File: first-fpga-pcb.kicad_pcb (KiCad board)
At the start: 4 copper layers, 34 parts, among them U1 iCE40-HX1K-VQ100, U2 W25Q128JVS, U3 TLV73312PDBV, U4 TLV73333PDBV, X1 SiT2001B

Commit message: neaten schematic
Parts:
- added C16: 100n, Capacitor_SMD:C_0805_2012Metric, F.Cu at (219.5, 87.8)
- added C17: 100n, Capacitor_SMD:C_0805_2012Metric, F.Cu at (215.1, 90.8)
- added C18: 100n, Capacitor_SMD:C_0805_2012Metric, F.Cu at (230.3, 75.1)
- added C19: 100n, Capacitor_SMD:C_0805_2012Metric, F.Cu at (225.9, 78.1)
- added D3: LED, LED_SMD:LED_0805_2012Metric, F.Cu at (189.4, 92.9)
- added D4: LED, LED_SMD:LED_0805_2012Metric, F.Cu at (215.1, 87.8)
- added D5: LED, LED_SMD:LED_0805_2012Metric, F.Cu at (225.9, 75.1)
- added J1: Conn_01x02, Connector_PinHeader_2.54mm:PinHeader_2x01_P2.54mm_Vertical, F.Cu at (226.0, 71.3)
- added J2: Conn_01x08, Connector_PinHeader_2.54mm:PinHeader_1x08_P2.54mm_Vertical, F.Cu at (189.4, 71.3)
- added J3: Conn_02x06_Top_Bottom, Connector_PinHeader_2.54mm:PinHeader_2x06_P2.54mm_Horizontal, F.Cu at (194.1, 71.3)
- added J4: Conn_02x06_Top_Bottom, Connector_PinHeader_2.54mm:PinHeader_2x06_P2.54mm_Horizontal, F.Cu at (210.0, 71.3)
- added R10: 10k, Resistor_SMD:R_0805_2012Metric, F.Cu at (215.1, 93.8)
- added R11: 10k, Resistor_SMD:R_0805_2012Metric, F.Cu at (230.3, 78.1)
- added R12: 200R, Resistor_SMD:R_0805_2012Metric, F.Cu at (219.5, 90.8)
- added R13: 200R, Resistor_SMD:R_0805_2012Metric, F.Cu at (225.9, 84.0)
- added R9: 22R, Resistor_SMD:R_0805_2012Metric, F.Cu at (225.9, 81.1)
- added SW1: SW_Push, Button_Switch_THT:SW_PUSH_6mm, F.Cu at (204.3, 88.3)
- added SW2: SW_Push, Button_Switch_THT:SW_PUSH_6mm, F.Cu at (193.8, 88.3)
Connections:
- net /reset renamed Net-(U1-Pad89)
- net Net-(D1-Pad2) renamed /cdone
- net Net-(R8-Pad1) renamed /creset
- C10 pad 1: +3V3 -> +1V2
- C11 pad 1: +3V3 -> +1V2
- C8 pad 1: +3V3 -> +1V2
- C9 pad 1: +3V3 -> +1V2
- U1 pad 1: Net-(U1-Pad1) -> /p2_1
- U1 pad 10: Net-(U1-Pad10) -> /p2_10
- U1 pad 2: Net-(U1-Pad2) -> /p2_2
- U1 pad 3: Net-(U1-Pad3) -> /p2_3
- U1 pad 4: Net-(U1-Pad4) -> /p2_4
- U1 pad 51: Net-(U1-Pad51) -> /p1_1
- U1 pad 52: Net-(U1-Pad52) -> /p1_2
- U1 pad 53: Net-(U1-Pad53) -> /p1_3
- U1 pad 54: Net-(U1-Pad54) -> /p1_4
- U1 pad 56: Net-(U1-Pad56) -> /p1_7
- U1 pad 57: Net-(U1-Pad57) -> /p1_8
- U1 pad 59: Net-(U1-Pad59) -> /p1_9
- U1 pad 60: Net-(U1-Pad60) -> /p1_10
- U1 pad 7: Net-(U1-Pad7) -> /p2_7
- U1 pad 78: Net-(U1-Pad78) -> /button1
- U1 pad 79: Net-(U1-Pad79) -> /button2
- U1 pad 8: Net-(U1-Pad8) -> /p2_8
- U1 pad 80: Net-(U1-Pad80) -> /led1
- U1 pad 81: Net-(U1-Pad81) -> /led2
- U1 pad 9: Net-(U1-Pad9) -> /p2_9
- U4 pad 2: Net-(U4-Pad2) -> GND

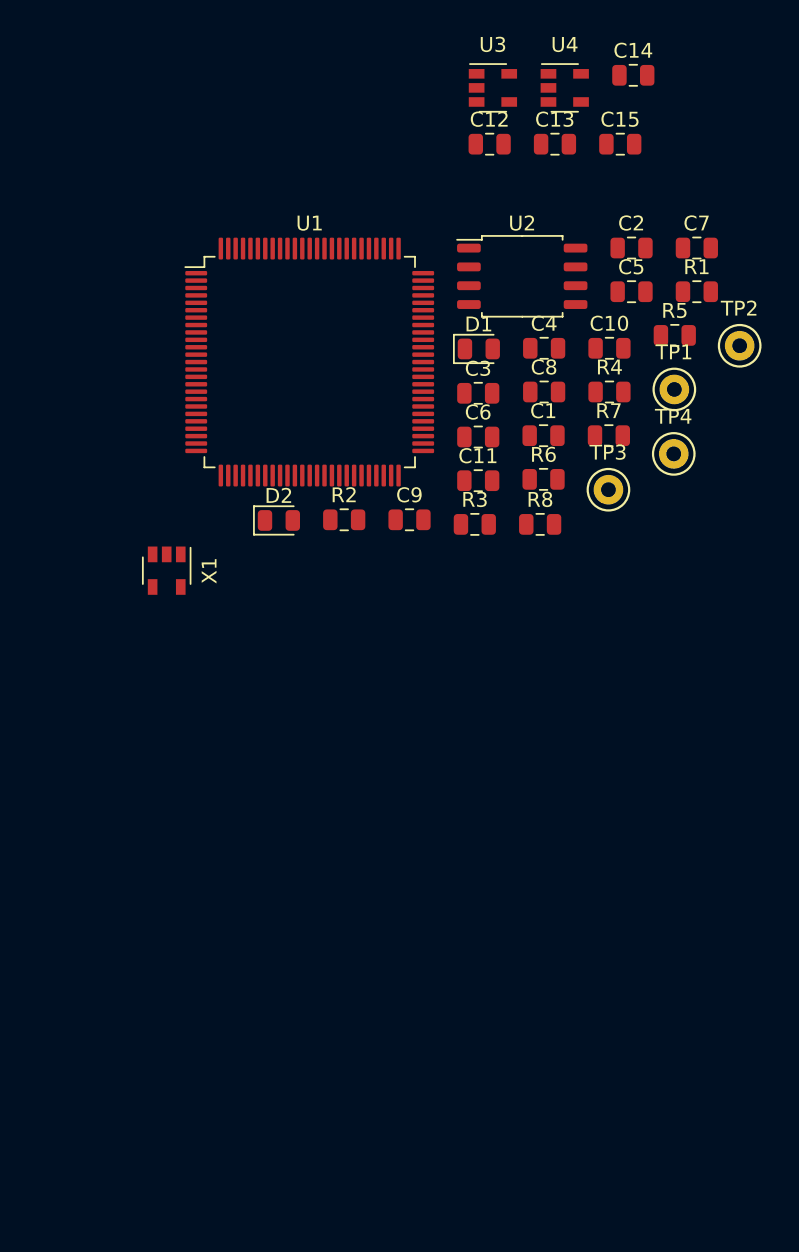
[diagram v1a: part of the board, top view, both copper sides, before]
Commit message: changed to 144 pin package for PLL, added more PMODs, chose FLASH part, updated README
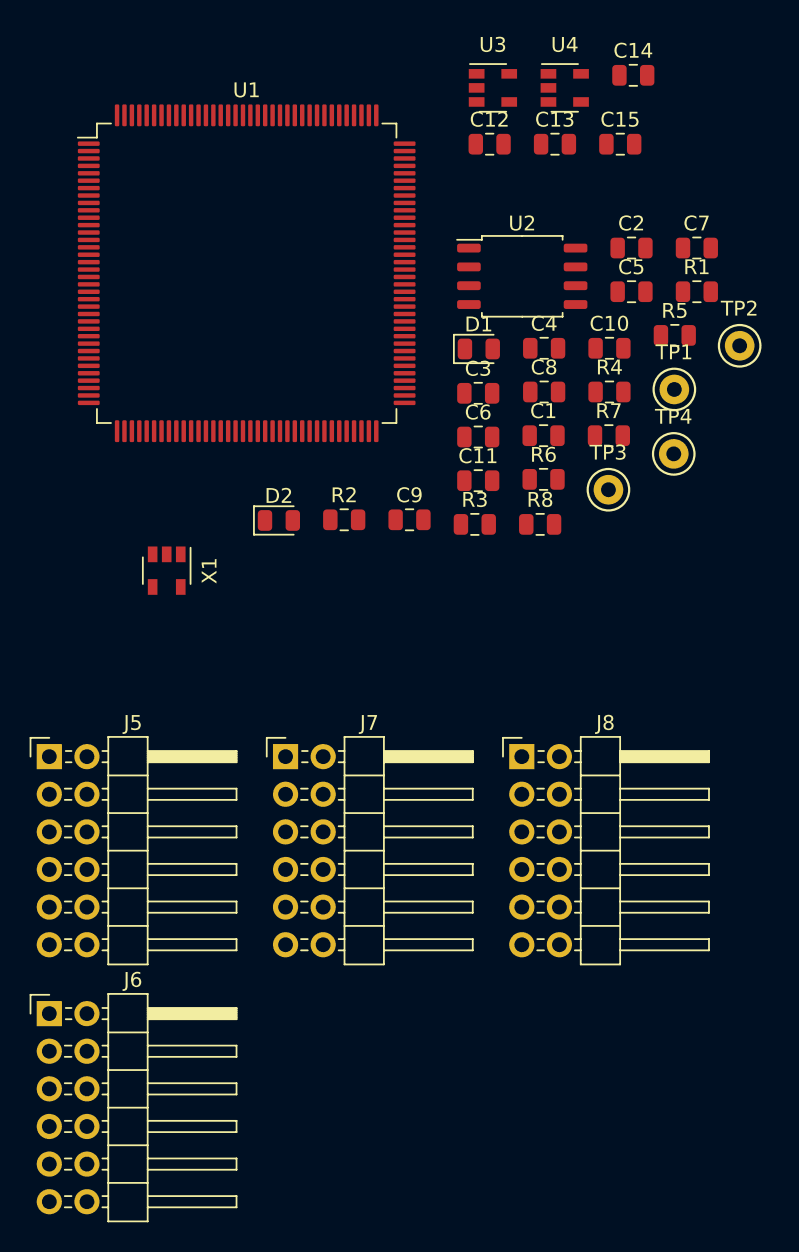
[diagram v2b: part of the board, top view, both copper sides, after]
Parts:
- added J5: Conn_02x06_Top_Bottom, Connector_PinHeader_2.54mm:PinHeader_2x06_P2.54mm_Horizontal, F.Cu at (134.1, 106.4)
- added J6: Conn_02x06_Top_Bottom, Connector_PinHeader_2.54mm:PinHeader_2x06_P2.54mm_Horizontal, F.Cu at (134.1, 123.7)
- added J7: Conn_02x06_Top_Bottom, Connector_PinHeader_2.54mm:PinHeader_2x06_P2.54mm_Horizontal, F.Cu at (150.1, 106.4)
- added J8: Conn_02x06_Top_Bottom, Connector_PinHeader_2.54mm:PinHeader_2x06_P2.54mm_Horizontal, F.Cu at (166.0, 106.4)
- R6: value 22R -> 200R
- U1: value iCE40-HX1K-VQ100 -> iCE40-HX1K-TQ144; footprint Package_QFP:VQFP-100_14x14mm_P0.5mm -> Package_QFP:TQFP-144_20x20mm_P0.5mm
- U2: value W25Q128JVS -> IS25LP016D-JBLE
- moved U1 7.35 mm to (147.5, 73.8)
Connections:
- U1 pad 1: /p2_1 -> /p3_1
- U1 pad 10: /p2_10 -> /p3_10
- U1 pad 100: Net-(U1-Pad100) -> +3V3
- U1 pad 11: +1V2 -> /p4_1
- U1 pad 12: Net-(U1-Pad12) -> /p4_2
- U1 pad 13: Net-(U1-Pad13) -> GND
- U1 pad 14: +3V3 -> GND
- U1 pad 17: GND -> Net-(U1-Pad17)
- U1 pad 19: Net-(U1-Pad19) -> /p4_3
- U1 pad 2: /p2_2 -> /p3_2
- U1 pad 20: Net-(U1-Pad20) -> /p4_4
- U1 pad 21: Net-(U1-Pad21) -> /p4_7
- U1 pad 22: +3V3 -> /p4_8
- U1 pad 23: GND -> /p4_9
- U1 pad 24: Net-(U1-Pad24) -> /p4_10
- U1 pad 27: Net-(U1-Pad27) -> +1V2
- U1 pad 3: /p2_3 -> /p3_3
- U1 pad 30: Net-(U1-Pad30) -> +3V3
- U1 pad 31: +3V3 -> Net-(U1-Pad31)
- U1 pad 32: GND -> Net-(U1-Pad32)
- U1 pad 33: Net-(TP1-Pad1) -> Net-(U1-Pad33)
- U1 pad 34: Net-(TP2-Pad1) -> Net-(U1-Pad34)
- U1 pad 35: +1V2 -> GND
- U1 pad 36: Net-(U1-Pad36) -> +1V2
- U1 pad 38: +3V3 -> Net-(U1-Pad38)
- U1 pad 39: GND -> Net-(U1-Pad39)
- U1 pad 4: /p2_4 -> /p3_4
- U1 pad 41: Net-(TP3-Pad1) -> Net-(U1-Pad41)
- U1 pad 42: Net-(TP4-Pad1) -> Net-(U1-Pad42)
- U1 pad 43: /cdone -> Net-(U1-Pad43)
- U1 pad 44: /creset -> Net-(TP1-Pad1)
- U1 pad 45: /sdo -> Net-(TP2-Pad1)
- U1 pad 46: /sdi -> +3V3
- U1 pad 47: GND -> Net-(U1-Pad47)
- U1 pad 48: /sd_clk -> Net-(U1-Pad48)
- U1 pad 49: /sd_cs -> Net-(U1-Pad49)
- U1 pad 50: +3V3 -> Net-(U1-Pad50)
- U1 pad 51: /p1_1 -> +1V2
- U1 pad 52: /p1_2 -> Net-(U1-Pad52)
- U1 pad 53: /p1_3 -> Net-(U1-Pad53)
- U1 pad 54: /p1_4 -> Net-(U1-Pad54)
- U1 pad 55: GND -> Net-(U1-Pad55)
- U1 pad 56: /p1_7 -> Net-(U1-Pad56)
- U1 pad 57: /p1_8 -> +3V3
- U1 pad 58: +3V3 -> Net-(U1-Pad58)
- U1 pad 59: /p1_9 -> GND
- U1 pad 60: /p1_10 -> Net-(U1-Pad60)
- U1 pad 61: +1V2 -> Net-(U1-Pad61)
- U1 pad 63: Net-(U1-Pad63) -> Net-(TP3-Pad1)
- U1 pad 64: Net-(U1-Pad64) -> Net-(TP4-Pad1)
- U1 pad 65: Net-(U1-Pad65) -> /cdone
- U1 pad 66: Net-(U1-Pad66) -> /creset
- U1 pad 67: +3V3 -> /sdo
- U1 pad 68: Net-(U1-Pad68) -> /sdi
- U1 pad 69: Net-(U1-Pad69) -> GND
- U1 pad 7: /p2_7 -> /p3_7
- U1 pad 70: GND -> /sd_clk
- U1 pad 71: Net-(U1-Pad71) -> /sd_cs
- U1 pad 72: Net-(U1-Pad72) -> +3V3
- U1 pad 73: Net-(U1-Pad73) -> /button1
- U1 pad 74: Net-(U1-Pad74) -> /button2
- U1 pad 75: Net-(D2-Pad1) -> /led1
- U1 pad 76: Net-(U1-Pad76) -> /led2
- U1 pad 77: +1V2 -> Net-(U1-Pad77)
- U1 pad 78: /button1 -> /p5_1
- U1 pad 79: /button2 -> /p5_2
- U1 pad 8: /p2_8 -> /p3_8
- U1 pad 80: /led1 -> /p5_3
- U1 pad 81: /led2 -> /p5_4
- U1 pad 84: GND -> Net-(U1-Pad84)
- U1 pad 86: Net-(U1-Pad86) -> GND
- U1 pad 87: Net-(U1-Pad87) -> /p5_7
- U1 pad 88: +3V3 -> /p5_8
- U1 pad 89: Net-(U1-Pad89) -> +3V3
- U1 pad 9: /p2_9 -> /p3_9
- U1 pad 90: /clock -> /p5_9
- U1 pad 91: Net-(U1-Pad91) -> /p5_10
- U1 pad 92: +3V3 -> +1V2
- U1 pad 93: Net-(U1-Pad93) -> /clock
- U1 pad 94: Net-(U1-Pad94) -> /p6_1
- U1 pad 95: Net-(U1-Pad95) -> /p6_2
- U1 pad 96: Net-(U1-Pad96) -> /p6_3
- U1 pad 97: Net-(U1-Pad97) -> /p6_4
- U1 pad 98: GND -> /p6_7
- U1 pad 99: Net-(U1-Pad99) -> /p6_8

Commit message: use submodule
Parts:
- R3: value 10k -> dnp
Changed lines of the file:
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@@
       (effects (font (size 1 1) (thickness 0.15)))
     )
-    (fp_text value 10k (at 0 1.65) (layer F.Fab)
+    (fp_text value dnp (at 0 1.65) (layer F.Fab)
       (effects (font (size 1 1) (thickness 0.15)))
     )

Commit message: starting layout
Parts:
- added C20: 100n, Capacitor_SMD:C_0805_2012Metric, F.Cu at (115.9, 99.1)
- added H1: MountingHole_Pad, MountingHole:MountingHole_3.2mm_M3_Pad, F.Cu at (80.0, 115.0)
- added H2: MountingHole_Pad, MountingHole:MountingHole_3.2mm_M3_Pad, F.Cu at (80.0, 55.0)
- added H3: MountingHole_Pad, MountingHole:MountingHole_3.2mm_M3_Pad, F.Cu at (170.0, 55.0)
- added H4: MountingHole_Pad, MountingHole:MountingHole_3.2mm_M3_Pad, F.Cu at (170.0, 115.0)
- added R14: 200R, Resistor_SMD:R_0805_2012Metric, F.Cu at (115.9, 102.0)
- added TP5: clock, TestPoint:TestPoint_THTPad_D1.0mm_Drill0.5mm, F.Cu at (108.0, 65.0)
- added TP6: 1.2v, TestPoint:TestPoint_THTPad_D1.0mm_Drill0.5mm, F.Cu at (147.5, 89.0)
- added TP7: 3.3v, TestPoint:TestPoint_THTPad_D1.0mm_Drill0.5mm, F.Cu at (138.0, 89.0)
- added TP8: 2.5v, TestPoint:TestPoint_THTPad_D1.0mm_Drill0.5mm, F.Cu at (97.0, 66.5)
- R9: value 22R -> 200R
- TP1, TP2, TP3, TP4: footprint TestPoint:TestPoint_Keystone_5000-5004_Miniature -> TestPoint:TestPoint_THTPad_D1.0mm_Drill0.5mm
- moved J4 133.8 mm to (80.0, 102.9), turned to 180 degrees
- moved C18 120.0 mm to (110.5, 68.1), turned to 90 degrees
- moved C16 119.6 mm to (100.5, 99.5), turned to 270 degrees
- moved J3 114.4 mm to (80.0, 80.0), turned to 180 degrees
- moved C19 102.9 mm to (123.0, 75.0)
- moved C17 102.4 mm to (113.0, 99.5), turned to 270 degrees
- moved D5 93.3 mm to (138.0, 106.5)
- moved R11 91.8 mm to (142.0, 103.5)
- moved R13 90.0 mm to (138.0, 103.5)
- moved C7 87.2 mm to (92.0, 87.0), turned to 180 degrees
- moved J7 77.4 mm to (91.4, 55.9), turned to 90 degrees
- moved C8 75.8 mm to (92.0, 76.0), turned to 180 degrees
- moved C4 75.6 mm to (92.0, 82.0), turned to 180 degrees
- moved J8 72.3 mm to (114.3, 55.9), turned to 90 degrees
- moved R12 72.1 mm to (148.5, 103.5)
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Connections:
- U1 pad 1: /p3_1 -> /p4_10
- U1 pad 10: /p3_10 -> /p4_1
- U1 pad 101: /p6_9 -> /p5_2
- U1 pad 102: /p6_10 -> /p5_1
- U1 pad 11: /p4_1 -> /p3_10
- U1 pad 112: /p1_1 -> /p1_10
- U1 pad 113: /p1_2 -> /p1_9
- U1 pad 114: /p1_3 -> /p1_8
- U1 pad 115: /p1_4 -> /p1_7
- U1 pad 116: /p1_7 -> /p1_4
- U1 pad 117: /p1_8 -> /p1_3
- U1 pad 118: /p1_9 -> /p1_2
- U1 pad 119: /p1_10 -> /p1_1
- U1 pad 12: /p4_2 -> /p3_9
- U1 pad 120: /p2_1 -> /p2_10
- U1 pad 121: /p2_2 -> /p2_9
- U1 pad 122: /p2_3 -> /p2_8
- U1 pad 128: /p2_4 -> /p2_7
- U1 pad 129: /p2_7 -> /p2_4
- U1 pad 134: /p2_8 -> /p2_3
- U1 pad 135: /p2_9 -> /p2_2
- U1 pad 136: /p2_10 -> /p2_1
- U1 pad 19: /p4_3 -> /p3_8
- U1 pad 2: /p3_2 -> /p4_9
- U1 pad 20: /p4_4 -> /p3_7
- U1 pad 21: /p4_7 -> /p3_4
- U1 pad 22: /p4_8 -> /p3_3
- U1 pad 23: /p4_9 -> /p3_2
- U1 pad 24: /p4_10 -> /p3_1
- U1 pad 3: /p3_3 -> /p4_8
- U1 pad 35: GND -> Net-(C20-Pad2)
- U1 pad 36: +1V2 -> /vcc_pll
- U1 pad 4: /p3_4 -> /p4_7
- U1 pad 7: /p3_7 -> /p4_4
- U1 pad 78: /p5_1 -> /p6_10
- U1 pad 79: /p5_2 -> /p6_9
- U1 pad 8: /p3_8 -> /p4_3
- U1 pad 80: /p5_3 -> /p6_8
- U1 pad 81: /p5_4 -> /p6_7
- U1 pad 87: /p5_7 -> /p6_4
- U1 pad 88: /p5_8 -> /p6_3
- U1 pad 9: /p3_9 -> /p4_2
- U1 pad 90: /p5_9 -> /p6_2
- U1 pad 91: /p5_10 -> /p6_1
- U1 pad 94: /p6_1 -> /p5_10
- U1 pad 95: /p6_2 -> /p5_9
- U1 pad 96: /p6_3 -> /p5_8
- U1 pad 97: /p6_4 -> /p5_7
- U1 pad 98: /p6_7 -> /p5_4
- U1 pad 99: /p6_8 -> /p5_3
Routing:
- net +3V3: track 0.00 -> 33.9 mm
- net +1V2: track 0.00 -> 11.9 mm
- net /vcc_pll: track 0.00 -> 5.05 mm
- net Net-(C20-Pad2): track 0.00 -> 4.72 mm
- net /creset: track 0.00 -> 4.42 mm
- added copper zone on B.Cu, net GND
- added copper zone on F.Cu, net GND
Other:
- board outline added: 100 x 70 mm
- copper layers 4 -> 2
- net class power added: clearance 0.16, trace_width 0.25, via_dia 0.6, via_drill 0.3
